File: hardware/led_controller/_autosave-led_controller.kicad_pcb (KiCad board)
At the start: 2 copper layers, 49.9 x 69.9 mm, 31 parts, among them J1 Header, J2 Header, J3 Header, J4 Header, J5 POWER, J6 Conn_01x02, U1 74AHCT125, U3 Waveshare ESP32-S3/C6 Zero

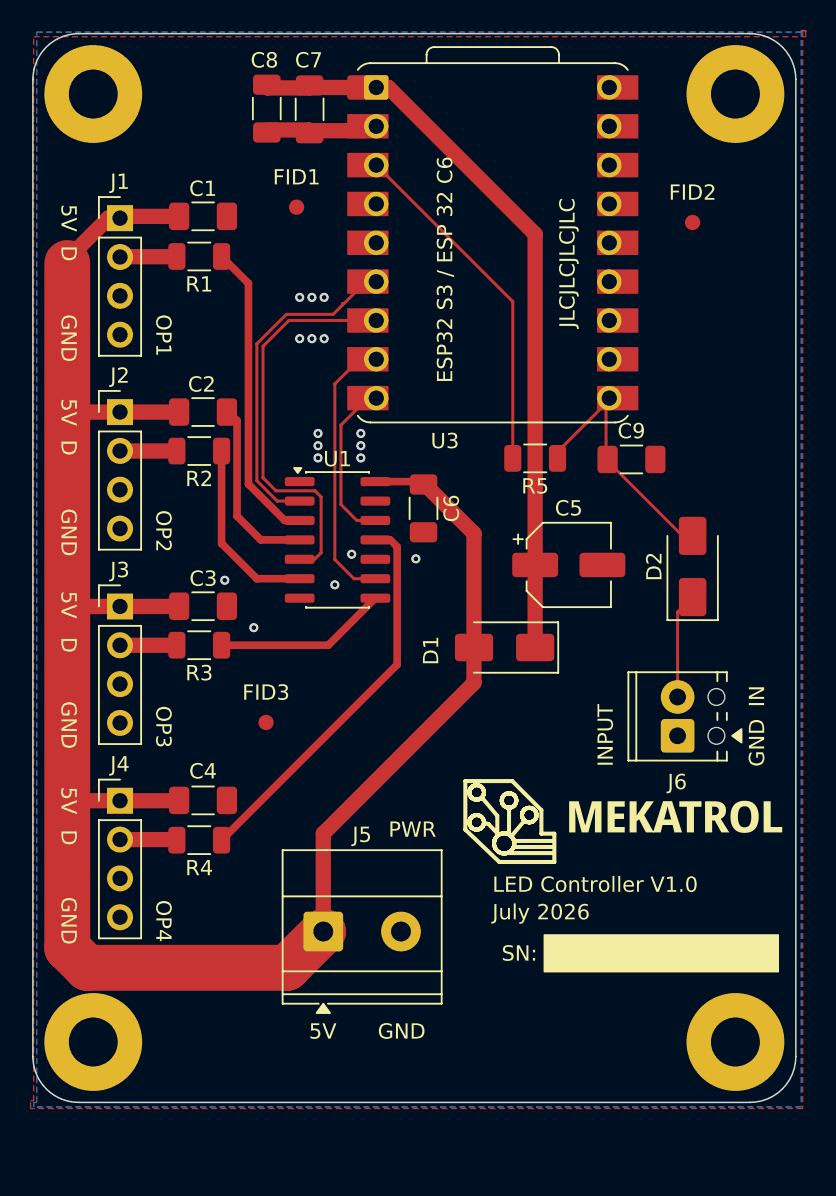
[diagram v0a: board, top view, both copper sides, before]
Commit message: Updating modules for layout edges, holes, etc
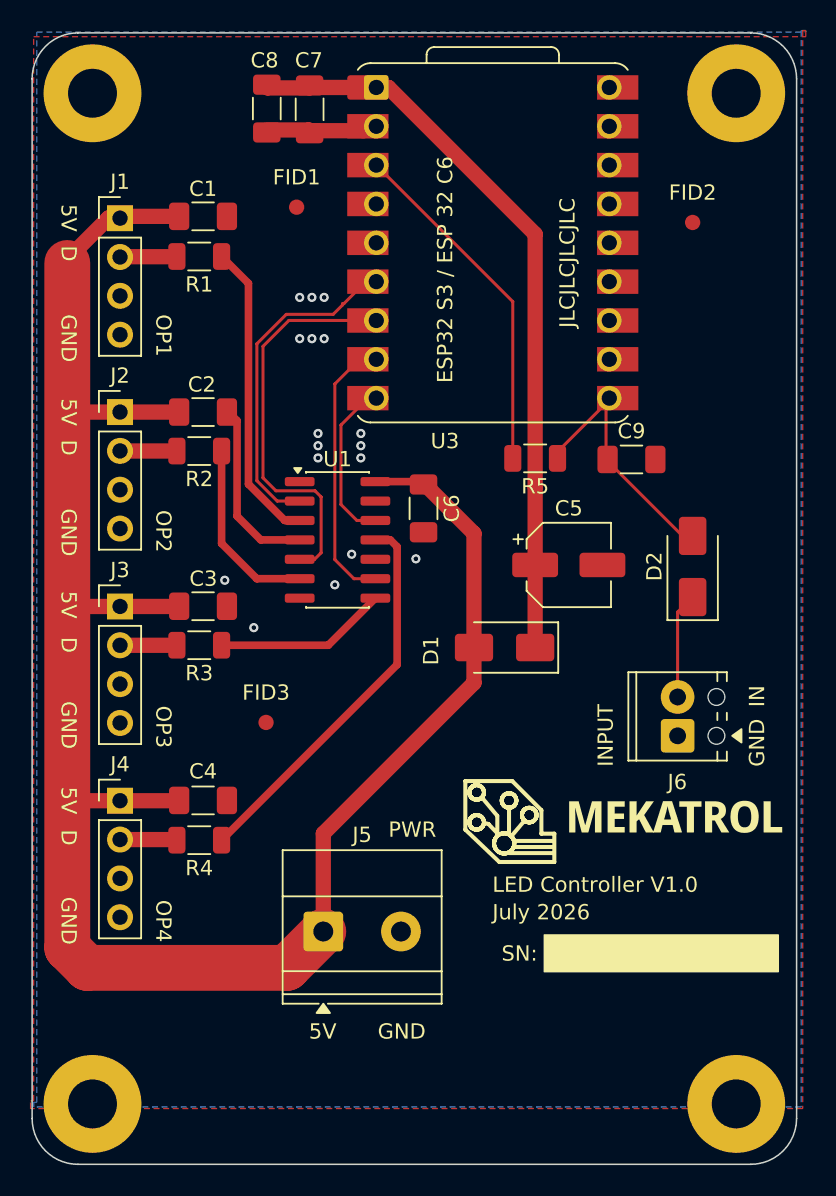
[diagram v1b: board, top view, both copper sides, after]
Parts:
- moved H3 4.05 mm to (124.0, 120.0)
- moved H4 4.05 mm to (166.1, 120.0)
- moved H2 0.07 mm to (166.1, 54.0)
- moved H1 0.07 mm to (124.0, 54.0)
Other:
- board size 49.9 x 69.9 mm -> 50 x 74 mm
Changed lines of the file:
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@@
 	(footprint "MountingHole:MountingHole_3.2mm_M3_Pad"
 		(layer "F.Cu")
-		(at 166 116)
+		(at 166.05 120.05)
 		(descr "Mounting Hole 3.2mm, M3, generated by kicad-footprint-generator mountinghole.py")
 		(tags "mountinghole M3")
@@
 	(footprint "MountingHole:MountingHole_3.2mm_M3_Pad"
 		(layer "F.Cu")
-		(at 166 54)
+		(at 166.05 53.95)
 		(descr "Mounting Hole 3.2mm, M3, generated by kicad-footprint-generator mountinghole.py")
 		(tags "mountinghole M3")
@@
 	(footprint "MountingHole:MountingHole_3.2mm_M3_Pad"
 		(layer "F.Cu")
-		(at 124 54)
+		(at 123.95 53.95)
 		(descr "Mounting Hole 3.2mm, M3, generated by kicad-footprint-generator mountinghole.py")
 		(tags "mountinghole M3")
@@
 	(footprint "MountingHole:MountingHole_3.2mm_M3_Pad"
 		(layer "F.Cu")
-		(at 124 116)
+		(at 123.95 120.05)
 		(descr "Mounting Hole 3.2mm, M3, generated by kicad-footprint-generator mountinghole.py")
 		(tags "mountinghole M3")
@@
 	)
 	(gr_arc
-		(start 120.05 53.05)
-		(mid 120.928679 50.928679)
-		(end 123.05 50.05)
+		(start 120 53)
+		(mid 120.878679 50.878679)
+		(end 123 50)
 		(stroke
 			(width 0.1)
@@
 	)
 	(gr_line
-		(start 120.05 116.95)
-		(end 120.05 53.05)
+		(start 120 121)
+		(end 120 53)
 		(stroke
 			(width 0.1)
@@
 	)
 	(gr_line
-		(start 123.05 50.05)
-		(end 166.95 50.05)
+		(start 123 50)
+		(end 167 50)
 		(stroke
 			(width 0.1)
@@
 	)
 	(gr_arc
-		(start 123.05 119.95)
-		(mid 120.928679 119.07132)
-		(end 120.05 116.95)
+		(start 123 124)
+		(mid 120.878679 123.12132)
+		(end 120 121)
 		(stroke
 			(width 0.1)
@@
 	)
 	(gr_arc
-		(start 166.95 50.05)
-		(mid 169.07132 50.928679)
-		(end 169.95 53.05)
+		(start 167 50)
+		(mid 169.12132 50.878679)
+		(end 170 53)
 		(stroke
 			(width 0.1)
@@
 	)
 	(gr_line
-		(start 166.95 119.95)
-		(end 123.05 119.95)
+		(start 167 124)
+		(end 123 124)
 		(stroke
 			(width 0.1)
@@
 	)
 	(gr_line
-		(start 169.95 53.05)
-		(end 169.95 116.95)
+		(start 170 53)
+		(end 170 121)
 		(stroke
 			(width 0.1)
@@
 	)
 	(gr_arc
-		(start 169.95 116.95)
-		(mid 169.07132 119.07132)
-		(end 166.95 119.95)
+		(start 170 121)
+		(mid 169.12132 123.12132)
+		(end 167 124)
 		(stroke
 			(width 0.1)

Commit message: Rebuild GND zones on edge cuts
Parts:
- moved H3 4.00 mm to (124.0, 116.0)
- moved H4 4.00 mm to (166.1, 116.0)
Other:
- board size 50 x 74 mm -> 50 x 70 mm
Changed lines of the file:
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@@
 	(footprint "MountingHole:MountingHole_3.2mm_M3_Pad"
 		(layer "F.Cu")
-		(at 166.05 120.05)
+		(at 166.05 116.05)
 		(descr "Mounting Hole 3.2mm, M3, generated by kicad-footprint-generator mountinghole.py")
 		(tags "mountinghole M3")
@@
 	(footprint "MountingHole:MountingHole_3.2mm_M3_Pad"
 		(layer "F.Cu")
-		(at 123.95 120.05)
+		(at 123.95 116.05)
 		(descr "Mounting Hole 3.2mm, M3, generated by kicad-footprint-generator mountinghole.py")
 		(tags "mountinghole M3")
@@
 	)
 	(gr_line
-		(start 120 121)
+		(start 120 117)
 		(end 120 53)
 		(stroke
@@
 	)
 	(gr_arc
-		(start 123 124)
-		(mid 120.878679 123.12132)
-		(end 120 121)
+		(start 123 120)
+		(mid 120.878679 119.12132)
+		(end 120 117)
 		(stroke
 			(width 0.1)
@@
 	)
 	(gr_line
-		(start 167 124)
-		(end 123 124)
+		(start 167 120)
+		(end 123 120)
 		(stroke
 			(width 0.1)
@@
 	(gr_line
 		(start 170 53)
-		(end 170 121)
+		(end 170 117)
 		(stroke
 			(width 0.1)
@@
 	)
 	(gr_arc
-		(start 170 121)
-		(mid 169.12132 123.12132)
-		(end 167 124)
+		(start 170 117)
+		(mid 169.12132 119.12132)
+		(end 167 120)
 		(stroke
 			(width 0.1)
@@
 	(zone
 		(net "GND")
-		(locked yes)
 		(layer "F.Cu")
 		(hatch edge 0.5)
-		(priority 1)
 		(connect_pads
 			(clearance 0.5)
@@
 		(polygon
 			(pts
-				(xy 120.1 50.25) (xy 170.6 50.25) (xy 170.6 49.85) (xy 170.4 49.85) (xy 170.4 120.35) (xy 119.9 120.35)
-				(xy 119.9 119.85) (xy 120.1 119.85)
+				(xy 120 50) (xy 170 50) (xy 170 120) (xy 120 120)
 			)
 		)
@@
 		(polygon
 			(pts
-				(xy 120.3 49.95) (xy 170.6 49.95) (xy 170.6 49.85) (xy 170.3 49.85) (xy 170.3 120.25) (xy 120.1 120.25)
-				(xy 120.1 119.95) (xy 120.3 119.95)
+				(xy 120 50) (xy 170 50) (xy 170 120) (xy 120 120)
 			)
 		)
